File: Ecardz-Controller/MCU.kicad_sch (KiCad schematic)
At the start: 0 parts

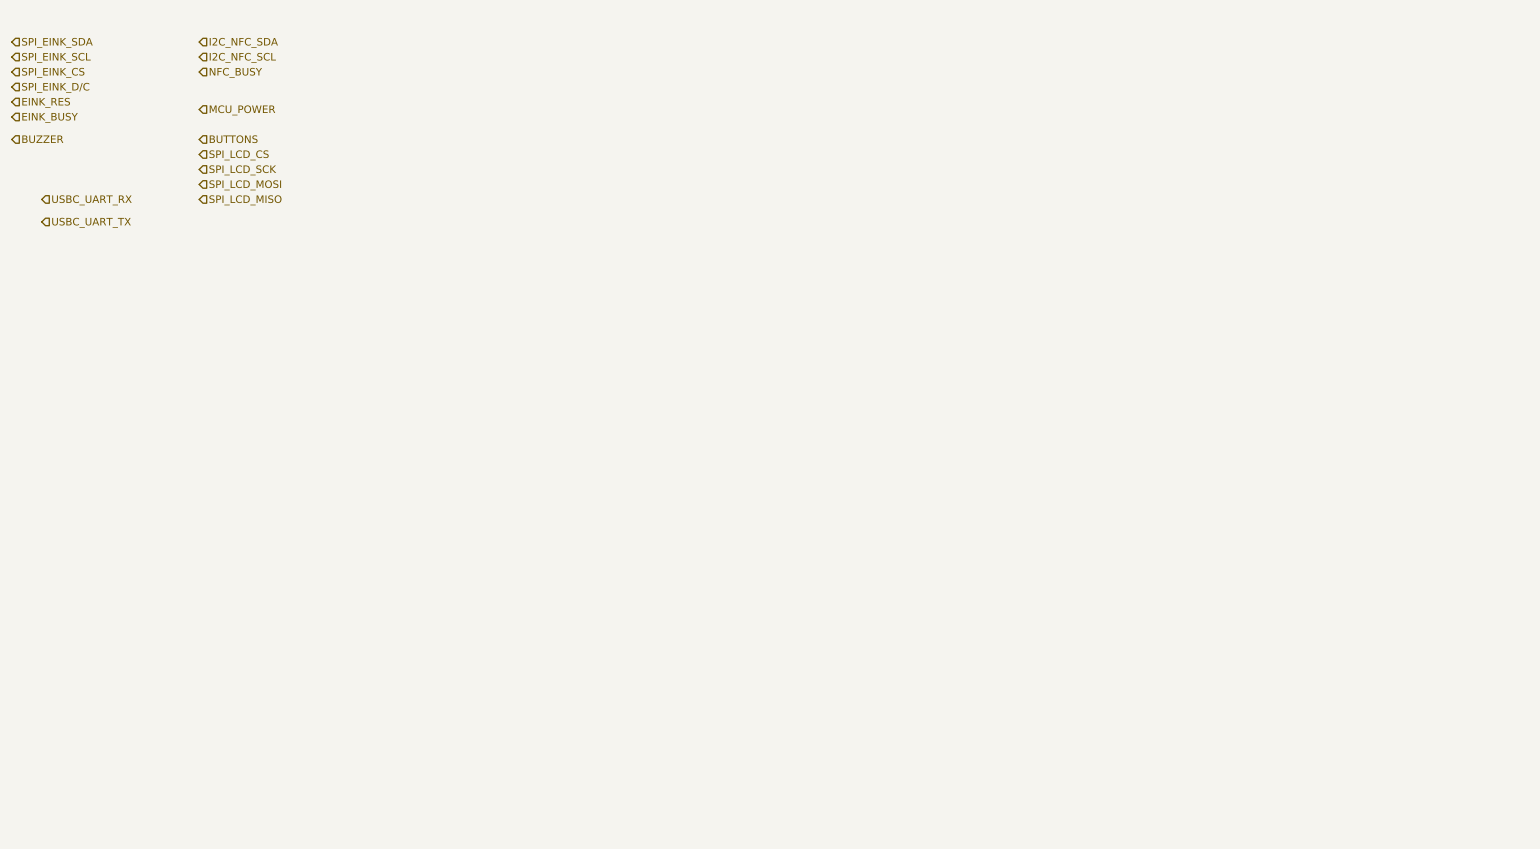
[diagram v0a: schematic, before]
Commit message: adding MCU
added peripheral connections as well as indicator lights
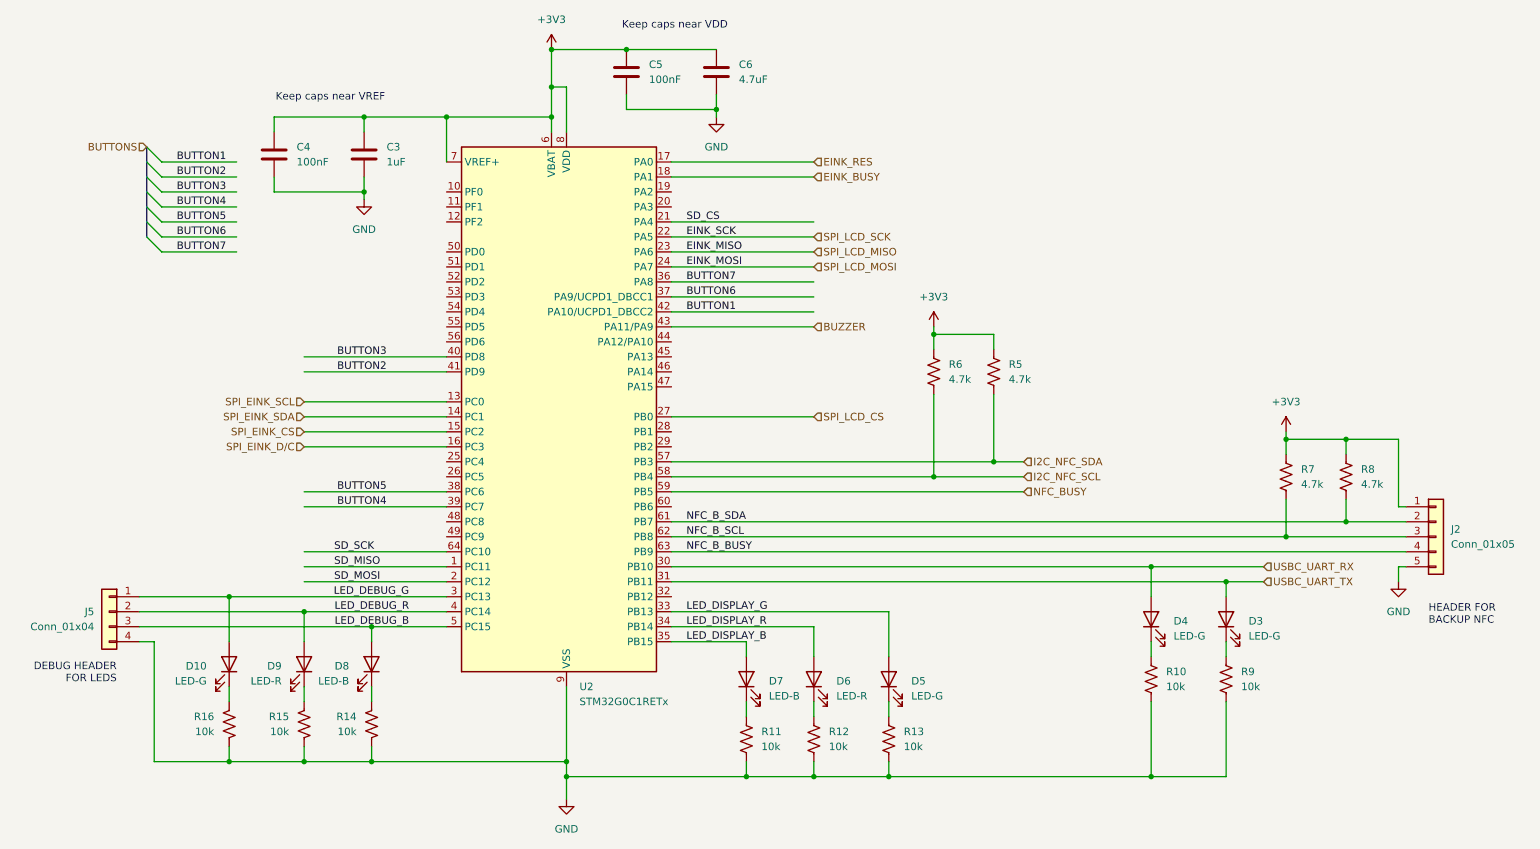
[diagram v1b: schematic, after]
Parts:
- added C3: 1uF, Capacitor_SMD:C_0603_1608Metric_Pad1.08x0.95mm_HandSolder, symbol Device:C
- added C4, C5: 100nF, Capacitor_SMD:C_0603_1608Metric_Pad1.08x0.95mm_HandSolder, symbol Device:C
- added C6: 4.7uF, Capacitor_SMD:C_0603_1608Metric_Pad1.08x0.95mm_HandSolder, symbol Device:C
- added D10, D3, D4, D5: LED-G, LED_SMD:LED_0603_1608Metric_Pad1.05x0.95mm_HandSolder, symbol Device:LED
- added D6, D9: LED-R, LED_SMD:LED_0603_1608Metric_Pad1.05x0.95mm_HandSolder, symbol Device:LED
- added D7, D8: LED-B, LED_SMD:LED_0603_1608Metric_Pad1.05x0.95mm_HandSolder, symbol Device:LED
- added J2: Conn_01x05, symbol Connector_Generic:Conn_01x05
- added J5: Conn_01x04, symbol Connector_Generic:Conn_01x04
- added R10, R11, R12, R13, R14, R15, R16, R9: 10k, Resistor_SMD:R_0603_1608Metric_Pad0.98x0.95mm_HandSolder, symbol Device:R_US
- added R5, R6, R7, R8: 4.7k, Resistor_SMD:R_0603_1608Metric_Pad0.98x0.95mm_HandSolder, symbol Device:R_US
- added U2: STM32G0C1RETx, Package_QFP:LQFP-64_10x10mm_P0.5mm, symbol MCU_ST_STM32G0:STM32G0C1RETx
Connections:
- net BUZZER: now also U2.43 (PA11/PA9)
- net EINK_BUSY: now also U2.18 (PA1)
- net EINK_RES: now also U2.17 (PA0)
- net I2C_NFC_SCL: now also R6.2, U2.58 (PB4)
- net I2C_NFC_SDA: now also R5.2, U2.57 (PB3)
- net NFC_BUSY: now also U2.59 (PB5)
- net SPI_EINK_CS: now also U2.15 (PC2)
- net SPI_EINK_D/C: now also U2.16 (PC3)
- net SPI_EINK_SCL: now also U2.13 (PC0)
- net SPI_EINK_SDA: now also U2.14 (PC1)
- net SPI_LCD_CS: now also U2.27 (PB0)
- net SPI_LCD_MISO: now also U2.23 (PA6)
- net SPI_LCD_MOSI: now also U2.24 (PA7)
- net SPI_LCD_SCK: now also U2.22 (PA5)
- net USBC_UART_RX: now also D4.2 (A), U2.30 (PB10)
- net USBC_UART_TX: now also D3.2 (A), U2.31 (PB11)
- new net: D9.1 (K), R15.1
- new net: D6.1 (K), R12.1
- new net: D7.1 (K), R11.1
- new net: D5.1 (K), R13.1
- new net: D4.1 (K), R10.1
- new net: D10.1 (K), R16.1
- new net: D3.1 (K), R9.1
- new net: D8.1 (K), R14.1
- new net +3V3: C3.1, C4.1, C5.1, C6.1, J2.1 (Pin_1), R5.1, R6.1, R7.1, R8.1, U2.6 (VBAT), U2.7 (VREF+), U2.8 (VDD)
- new net BUTTON1: U2.42 (PA10/UCPD1_DBCC2)
- new net BUTTON2: U2.41 (PD9)
- new net BUTTON3: U2.40 (PD8)
- new net BUTTON4: U2.39 (PC7)
- new net BUTTON5: U2.38 (PC6)
- new net BUTTON6: U2.37 (PA9/UCPD1_DBCC1)
- new net BUTTON7: U2.36 (PA8)
- new net GND: C3.2, C4.2, C5.2, C6.2, J2.5 (Pin_5), J5.4 (Pin_4), R10.2, R11.2, R12.2, R13.2, R14.2, R15.2, R16.2, R9.2, U2.9 (VSS)
- new net LED_DEBUG_B: D8.2 (A), J5.3 (Pin_3), U2.5 (PC15)
- new net LED_DEBUG_G: D10.2 (A), J5.1 (Pin_1), U2.3 (PC13)
- new net LED_DEBUG_R: D9.2 (A), J5.2 (Pin_2), U2.4 (PC14)
- new net LED_DISPLAY_B: D7.2 (A), U2.35 (PB15)
- new net LED_DISPLAY_G: D5.2 (A), U2.33 (PB13)
- new net LED_DISPLAY_R: D6.2 (A), U2.34 (PB14)
- new net NFC_B_BUSY: J2.4 (Pin_4), U2.63 (PB9)
- new net NFC_B_SCL: J2.3 (Pin_3), R7.2, U2.62 (PB8)
- new net NFC_B_SDA: J2.2 (Pin_2), R8.2, U2.61 (PB7)
- new net SD_CS: U2.21 (PA4)
- new net SD_MISO: U2.1 (PC11)
- new net SD_MOSI: U2.2 (PC12)
- new net SD_SCK: U2.64 (PC10)
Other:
- note added: "DEBUG HEADER FOR LEDS"
- note added: "HEADER FOR BACKUP NFC"
- note added: "Keep caps near VDD"
- note added: "Keep caps near VREF"

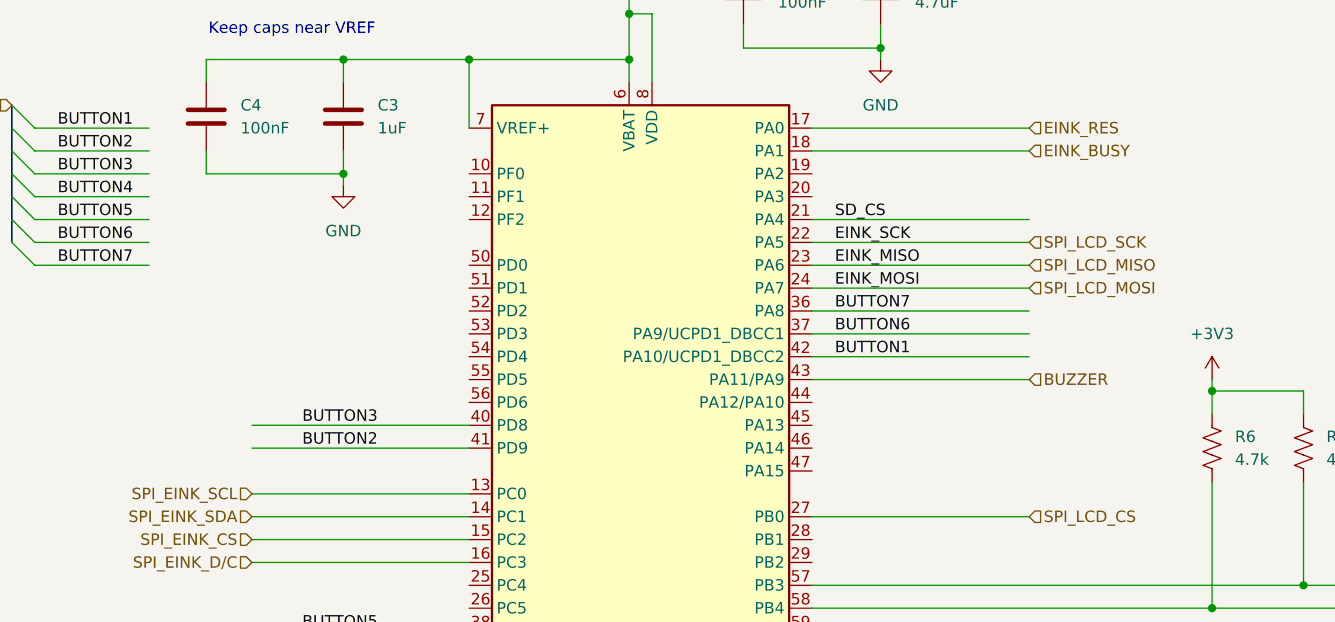
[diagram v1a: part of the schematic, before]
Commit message: updated button pin choices, updated root
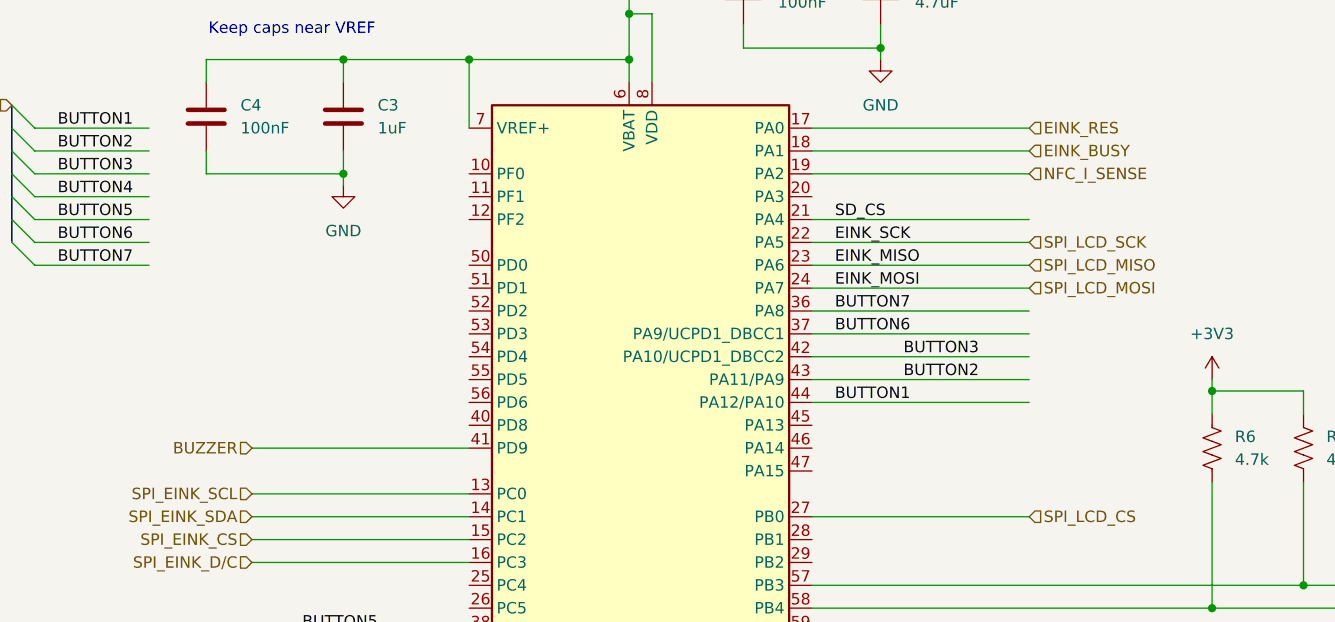
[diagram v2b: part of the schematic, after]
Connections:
- net BUTTON1: now also U2.44 (PA12/PA10); no longer U2.42 (PA10/UCPD1_DBCC2)
- net BUTTON2: now also U2.43 (PA11/PA9); no longer U2.41 (PD9)
- net BUTTON3: now also U2.42 (PA10/UCPD1_DBCC2); no longer U2.40 (PD8)
- net BUZZER: now also U2.41 (PD9); no longer U2.43 (PA11/PA9)
- net NFC_I_SENSE: now reaches U2.19 (PA2)
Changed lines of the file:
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@@
+	(wire
+		(pts
+			(xy 99.06 81.28) (xy 74.93 81.28)
+		)
+		(stroke
+			(width 0)
+			(type default)
+		)
+	)
 	(wire
 		(pts
@@
 	(wire
 		(pts
-			(xy 74.93 81.28) (xy 99.06 81.28)
-		)
-		(stroke
-			(width 0)
-			(type default)
-		)
-	)
-	(wire
-		(pts
-			(xy 74.93 78.74) (xy 99.06 78.74)
+			(xy 137.16 50.8) (xy 161.29 50.8)
 		)
 		(stroke
@@
 	(wire
 		(pts
-			(xy 137.16 71.12) (xy 161.29 71.12)
-		)
-		(stroke
-			(width 0)
-			(type default)
-		)
-	)
-	(wire
-		(pts
 			(xy 129.54 26.67) (xy 144.78 26.67)
 		)
@@
 	(wire
 		(pts
+			(xy 137.16 76.2) (xy 161.29 76.2)
+		)
+		(stroke
+			(width 0)
+			(type default)
+		)
+	)
+	(wire
+		(pts
 			(xy 137.16 55.88) (xy 161.29 55.88)
 		)
@@
 	(wire
 		(pts
+			(xy 161.29 73.66) (xy 137.16 73.66)
+		)
+		(stroke
+			(width 0)
+			(type default)
+		)
+	)
+	(wire
+		(pts
 			(xy 161.29 137.16) (xy 161.29 139.7)
 		)
@@
 	(wire
 		(pts
+			(xy 161.29 71.12) (xy 137.16 71.12)
+		)
+		(stroke
+			(width 0)
+			(type default)
+		)
+	)
+	(wire
+		(pts
 			(xy 74.93 93.98) (xy 99.06 93.98)
 		)
@@
 		(pts
 			(xy 144.78 34.29) (xy 144.78 36.83)
-		)
-		(stroke
-			(width 0)
-			(type default)
-		)
-	)
-	(wire
-		(pts
-			(xy 137.16 73.66) (xy 161.29 73.66)
 		)
 		(stroke
@@
 		)
 	)
+	(label "BUTTON2"
+		(at 147.32 73.66 0)
+		(fields_autoplaced yes)
+		(effects
+			(font
+				(size 1.27 1.27)
+			)
+			(justify left bottom)
+		)
+	)
 	(label "EINK_MISO"
 		(at 139.7 60.96 0)
@@
 		)
 	)
+	(label "BUTTON3"
+		(at 147.32 71.12 0)
+		(fields_autoplaced yes)
+		(effects
+			(font
+				(size 1.27 1.27)
+			)
+			(justify left bottom)
+		)
+	)
 	(label "BUTTON4"
 		(at 88.9 104.14 180)
@@
 		)
 	)
-	(label "BUTTON2"
-		(at 88.9 81.28 180)
-		(fields_autoplaced yes)
-		(effects
-			(font
-				(size 1.27 1.27)
-			)
-			(justify right bottom)
+	(label "BUTTON1"
+		(at 139.7 76.2 0)
+		(fields_autoplaced yes)
+		(effects
+			(font
+				(size 1.27 1.27)
+			)
+			(justify left bottom)
 		)
 	)
@@
 		)
 	)
-	(label "BUTTON3"
-		(at 88.9 78.74 180)
-		(fields_autoplaced yes)
-		(effects
-			(font
-				(size 1.27 1.27)
-			)
-			(justify right bottom)
-		)
-	)
 	(label "SD_MISO"
 		(at 80.01 114.3 0)
@@
 		)
 	)
-	(label "BUTTON1"
-		(at 139.7 71.12 0)
-		(fields_autoplaced yes)
-		(effects
-			(font
-				(size 1.27 1.27)
-			)
-			(justify left bottom)
-		)
-	)
 	(label "BUTTON6"
 		(at 53.34 58.42 0)
@@
 		)
 	)
+	(hierarchical_label "BUZZER"
+		(shape input)
+		(at 74.93 81.28 180)
+		(fields_autoplaced yes)
+		(effects
+			(font
+				(size 1.27 1.27)
+			)
+			(justify right)
+		)
+	)
 	(hierarchical_label "BUTTONS"
 		(shape input)
@@
 		)
 	)
+	(hierarchical_label "NFC_I_SENSE"
+		(shape input)
+		(at 161.29 50.8 0)
+		(fields_autoplaced yes)
+		(effects
+			(font
+				(size 1.27 1.27)
+			)
+			(justify left)
+		)
+	)
 	(hierarchical_label "USBC_UART_TX"
 		(shape input)
@@
 		)
 	)
-	(hierarchical_label "BUZZER"
-		(shape input)
-		(at 161.29 73.66 0)
-		(fields_autoplaced yes)
-		(effects
-			(font
-				(size 1.27 1.27)
-			)
-			(justify left)
-		)
-	)
